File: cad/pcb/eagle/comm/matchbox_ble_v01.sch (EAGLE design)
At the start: 24 parts, among them J1 DF12-32-DS, J2 DF12-32-DS, P1 DF12-32-DP, P2 DF12-32-DP, U1 NRF8001, U5 2450BM14A0002, Y1 NX3225SA-16

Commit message: BT tweaks
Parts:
- removed TP1, TP2, TP3: TEST-POINT3X5, SparkFun-Passives:TEST-POINT3X5
- added R3, R4, R5: 0K, SparkFun-Passives:RESISTOR0805-RES
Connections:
- net N$3 renamed ANT2
- net N$6 renamed ANT1
- net ACTIVE: no longer TP1.1
- net PA9: now also R3.1
- net PB3: now also U1.SCK
- net PB4: now also U1.MISO
- net PB5: now also U1.MOSI
- net PB6: now also R4.1
- net PB7: now also R5.1
- net PC10: no longer U1.SCK
- net PC11: no longer U1.MISO
- net PC12: no longer U1.MOSI
- net RDYN: now also R3.2
- net RXD: now also R4.2; no longer TP2.1
- net TXD: now also R5.2; no longer TP3.1

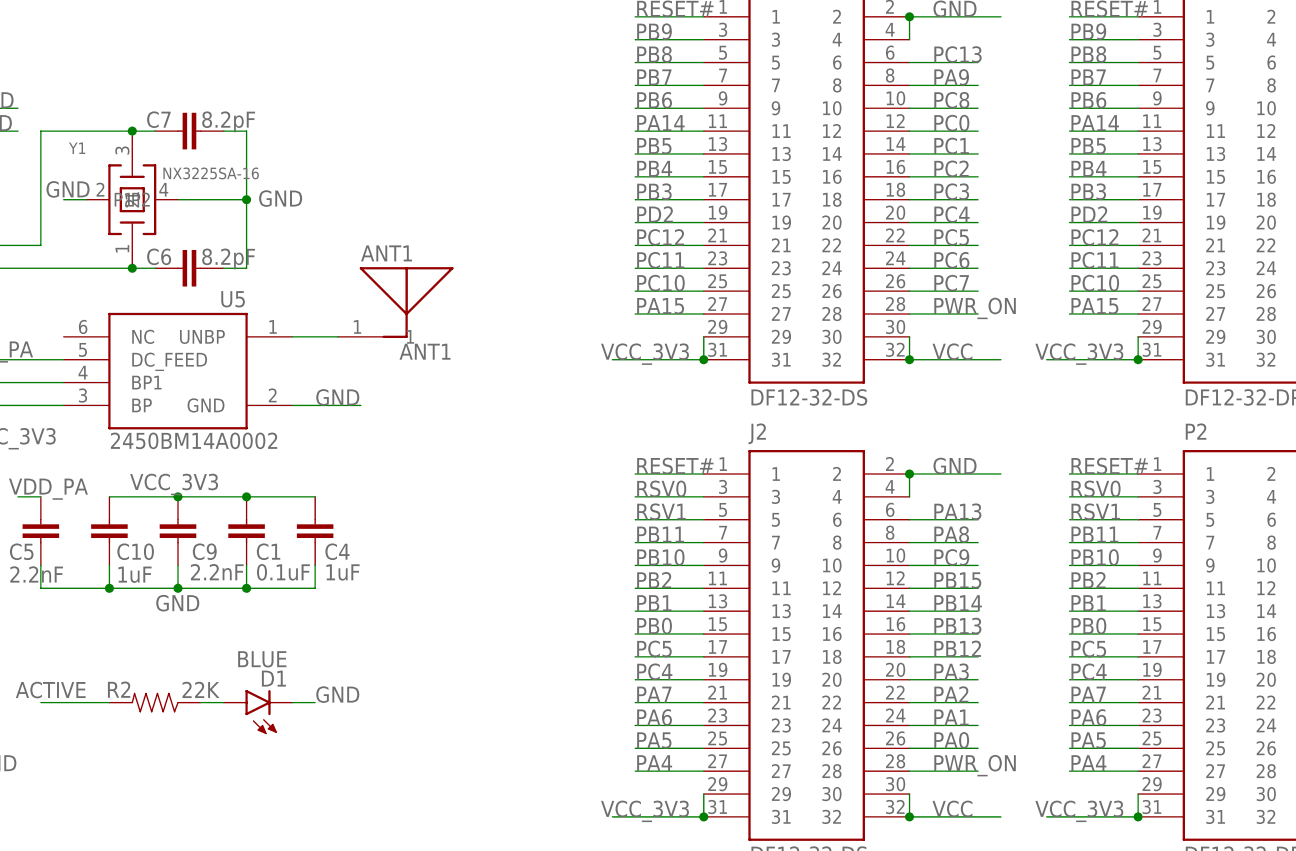
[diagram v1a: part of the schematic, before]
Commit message: Switch BLE to 40x32mm form factor
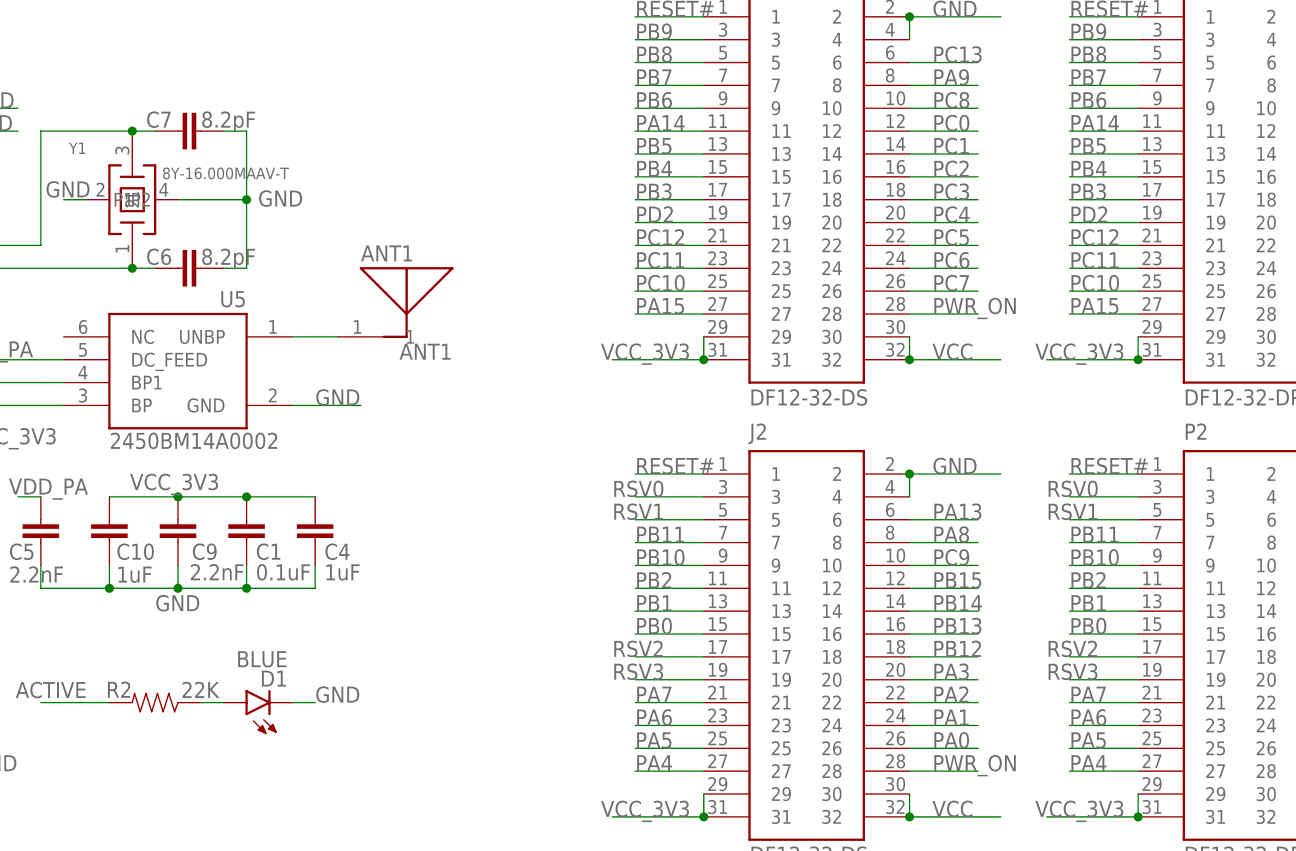
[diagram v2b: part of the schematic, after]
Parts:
- Y1: value NX3225SA-16 -> 8Y-16.000MAAV-T; device tinycircuits:AS-ITM-00228 -> micro1292:AS-ITM-00228
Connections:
- new net RSV2: J2.17, P2.17
- new net RSV3: J2.19, P2.19
- net PC4: no longer J2.19, P2.19
- net PC5: no longer J2.17, P2.17
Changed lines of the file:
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@@
 <layer number="115" name="ReferenceISLANDS" color="7" fill="1" visible="yes" active="yes"/>
 <layer number="116" name="Patch_BOT" color="7" fill="1" visible="yes" active="yes"/>
+<layer number="117" name="mPads" color="7" fill="1" visible="yes" active="yes"/>
 <layer number="118" name="Rect_Pads" color="7" fill="1" visible="yes" active="yes"/>
+<layer number="119" name="mUnrouted" color="7" fill="1" visible="yes" active="yes"/>
+<layer number="120" name="mDimension" color="7" fill="1" visible="yes" active="yes"/>
 <layer number="121" name="_tsilk" color="7" fill="1" visible="yes" active="yes"/>
 <layer number="122" name="_bsilk" color="7" fill="1" visible="yes" active="yes"/>
@@
 <layer number="128" name="_bValues" color="7" fill="1" visible="yes" active="yes"/>
 <layer number="129" name="Mask" color="7" fill="1" visible="yes" active="yes"/>
+<layer number="130" name="mbStop" color="7" fill="1" visible="yes" active="yes"/>
 <layer number="131" name="tAdjust" color="7" fill="1" visible="yes" active="yes"/>
 <layer number="132" name="bAdjust" color="7" fill="1" visible="yes" active="yes"/>
+<layer number="133" name="mtFinish" color="7" fill="1" visible="yes" active="yes"/>
+<layer number="134" name="mbFinish" color="7" fill="1" visible="yes" active="yes"/>
+<layer number="135" name="mtGlue" color="7" fill="1" visible="yes" active="yes"/>
+<layer number="136" name="mbGlue" color="7" fill="1" visible="yes" active="yes"/>
+<layer number="137" name="mtTest" color="7" fill="1" visible="yes" active="yes"/>
+<layer number="138" name="mbTest" color="7" fill="1" visible="yes" active="yes"/>
+<layer number="139" name="mtKeepout" color="7" fill="1" visible="yes" active="yes"/>
+<layer number="140" name="mbKeepout" color="7" fill="1" visible="yes" active="yes"/>
+<layer number="141" name="mtRestrict" color="7" fill="1" visible="yes" active="yes"/>
+<layer number="142" name="mbRestrict" color="7" fill="1" visible="yes" active="yes"/>
+<layer number="143" name="mvRestrict" color="7" fill="1" visible="yes" active="yes"/>
 <layer number="144" name="Drill_legend" color="7" fill="1" visible="yes" active="yes"/>
+<layer number="145" name="mHoles" color="7" fill="1" visible="yes" active="yes"/>
+<layer number="146" name="mMilling" color="7" fill="1" visible="yes" active="yes"/>
+<layer number="147" name="mMeasures" color="7" fill="1" visible="yes" active="yes"/>
+<layer number="148" name="mDocument" color="7" fill="1" visible="yes" active="yes"/>
+<layer number="149" name="mReference" color="7" fill="1" visible="yes" active="yes"/>
 <layer number="150" name="Notes" color="7" fill="1" visible="yes" active="yes"/>
 <layer number="151" name="HeatSink" color="7" fill="1" visible="yes" active="yes"/>
@@
 <layer number="154" name="FabDoc2" color="7" fill="1" visible="yes" active="yes"/>
 <layer number="155" name="FabDoc3" color="7" fill="1" visible="yes" active="yes"/>
+<layer number="191" name="mNets" color="7" fill="1" visible="yes" active="yes"/>
+<layer number="192" name="mBusses" color="7" fill="1" visible="yes" active="yes"/>
+<layer number="193" name="mPins" color="7" fill="1" visible="yes" active="yes"/>
+<layer number="194" name="mSymbols" color="7" fill="1" visible="yes" active="yes"/>
+<layer number="195" name="mNames" color="7" fill="1" visible="yes" active="yes"/>
+<layer number="196" name="mValues" color="7" fill="1" visible="yes" active="yes"/>
 <layer number="199" name="Contour" color="7" fill="1" visible="yes" active="yes"/>
 <layer number="200" name="200bmp" color="7" fill="1" visible="yes" active="yes"/>
@@
 <part name="U5" library="tinycircuits" deviceset="AS-ITM-00114" device="" value="2450BM14A0002"/>
 <part name="C5" library="SparkFun-Passives" deviceset="CAP" device="0402-CAP" value="2.2nF"/>
-<part name="Y1" library="tinycircuits" deviceset="AS-ITM-00228" device="" value="NX3225SA-16">
+<part name="Y1" library="micro1292" deviceset="AS-ITM-00228" device="" value="8Y-16.000MAAV-T">
 <attribute name="PARTNO" value="AS-ITM-00228"/>
 <attribute name="VALUE" value="8Y-16.000MAAV-T"/>
@@
 <net name="PC4" class="0">
 <segment>
-<wire x1="167.64" y1="48.26" x2="175.26" y2="48.26" width="0.1524" layer="91"/>
-<label x="167.64" y="48.26" size="1.778" layer="95"/>
-<pinref part="P2" gate="G$1" pin="19"/>
-</segment>
-<segment>
 <wire x1="198.12" y1="99.06" x2="205.74" y2="99.06" width="0.1524" layer="91"/>
 <label x="200.66" y="99.06" size="1.778" layer="95"/>
@@
 </segment>
 <segment>
-<wire x1="119.38" y1="48.26" x2="127" y2="48.26" width="0.1524" layer="91"/>
-<label x="119.38" y="48.26" size="1.778" layer="95"/>
-<pinref part="J2" gate="G$1" pin="19"/>
-</segment>
-<segment>
 <wire x1="149.86" y1="99.06" x2="157.48" y2="99.06" width="0.1524" layer="91"/>
 <label x="152.4" y="99.06" size="1.778" layer="95"/>
@@
 <net name="PC5" class="0">
 <segment>
-<wire x1="167.64" y1="50.8" x2="175.26" y2="50.8" width="0.1524" layer="91"/>
-<label x="167.64" y="50.8" size="1.778" layer="95"/>
-<pinref part="P2" gate="G$1" pin="17"/>
-</segment>
-<segment>
 <wire x1="198.12" y1="96.52" x2="205.74" y2="96.52" width="0.1524" layer="91"/>
 <label x="200.66" y="96.52" size="1.778" layer="95"/>
@@
 </segment>
 <segment>
-<wire x1="119.38" y1="50.8" x2="127" y2="50.8" width="0.1524" layer="91"/>
-<label x="119.38" y="50.8" size="1.778" layer="95"/>
-<pinref part="J2" gate="G$1" pin="17"/>
-</segment>
-<segment>
 <wire x1="149.86" y1="96.52" x2="157.48" y2="96.52" width="0.1524" layer="91"/>
 <label x="152.4" y="96.52" size="1.778" layer="95"/>
@@
 <segment>
 <wire x1="167.64" y1="68.58" x2="175.26" y2="68.58" width="0.1524" layer="91"/>
-<label x="167.64" y="68.58" size="1.778" layer="95"/>
+<label x="165.1" y="68.58" size="1.778" layer="95"/>
 <pinref part="P2" gate="G$1" pin="3"/>
 </segment>
 <segment>
 <wire x1="119.38" y1="68.58" x2="127" y2="68.58" width="0.1524" layer="91"/>
-<label x="119.38" y="68.58" size="1.778" layer="95"/>
+<label x="116.84" y="68.58" size="1.778" layer="95"/>
 <pinref part="J2" gate="G$1" pin="3"/>
 </segment>
@@
 <segment>
 <wire x1="167.64" y1="66.04" x2="175.26" y2="66.04" width="0.1524" layer="91"/>
-<label x="167.64" y="66.04" size="1.778" layer="95"/>
+<label x="165.1" y="66.04" size="1.778" layer="95"/>
 <pinref part="P2" gate="G$1" pin="5"/>
 </segment>
 <segment>
 <wire x1="119.38" y1="66.04" x2="127" y2="66.04" width="0.1524" layer="91"/>
-<label x="119.38" y="66.04" size="1.778" layer="95"/>
+<label x="116.84" y="66.04" size="1.778" layer="95"/>
 <pinref part="J2" gate="G$1" pin="5"/>
 </segment>
@@
 </segment>
 </net>
+<net name="RSV2" class="0">
+<segment>
+<wire x1="119.38" y1="50.8" x2="127" y2="50.8" width="0.1524" layer="91"/>
+<label x="116.84" y="50.8" size="1.778" layer="95"/>
+<pinref part="J2" gate="G$1" pin="17"/>
+</segment>
+<segment>
+<wire x1="167.64" y1="50.8" x2="175.26" y2="50.8" width="0.1524" layer="91"/>
+<label x="165.1" y="50.8" size="1.778" layer="95"/>
+<pinref part="P2" gate="G$1" pin="17"/>
+</segment>
+</net>
+<net name="RSV3" class="0">
+<segment>
+<wire x1="119.38" y1="48.26" x2="127" y2="48.26" width="0.1524" layer="91"/>
+<label x="116.84" y="48.26" size="1.778" layer="95"/>
+<pinref part="J2" gate="G$1" pin="19"/>
+</segment>
+<segment>
+<wire x1="167.64" y1="48.26" x2="175.26" y2="48.26" width="0.1524" layer="91"/>
+<label x="165.1" y="48.26" size="1.778" layer="95"/>
+<pinref part="P2" gate="G$1" pin="19"/>
+</segment>
+</net>

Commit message: Add VDDA supply (WIP)
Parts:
- added C8: 0.1µF, SparkFun-Capacitors:CAP0805
- added FB1: MMZ1608B121C, microbuilder:FERRITE0805
- added L4: 10µH, microbuilder:INDUCTOR_0603
- added L5: 15nH, microbuilder:INDUCTOR_0603
- added R6: 0K, SparkFun-Passives:RESISTOR0805-RES
- R2: value 22K -> 1K; device SparkFun-Passives:RESISTOR0402-RES -> SparkFun-Passives:RESISTOR0805-RES
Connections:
- new net AVDD: C8.1, FB1.P$2, L5.2, U1.AVDD, U1.AVDD1, U1.AVDD2
- new net DCC: L4.1, U1.DCC
- new net DET: R6.2, U$1.DET
- new net N$3: L4.2, L5.1
- net GND: now also C8.2
- net PB8: now also R6.1
- net VCC_3V3: now also FB1.P$1; no longer U1.AVDD, U1.AVDD1, U1.AVDD2
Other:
- moved on the sheet: D1, J1, J2, P1, P2, R2, U$1

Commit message: Final BLE board
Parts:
- removed C8: 0.1µF, SparkFun-Capacitors:CAP0805
- removed FB1: MMZ1608B121C, microbuilder:FERRITE0805
- removed L4: 10µH, microbuilder:INDUCTOR_0603
- removed L5: 15nH, microbuilder:INDUCTOR_0603
- ANT1, C2, C4, C5, C6, C7, D1, J1, J2, P1, P2, R1, R2, R3, R4, R5, R6, U$1, U1, U5, Y1: OC_NEWARK (none) -> unknown
- C1, C3: value 0.1uF -> 100nF; MF (none) -> VISHAY/SPRAGUE; MPN (none) -> 1C20Z5U104M050B; OC_NEWARK (none) -> 17F2165
- C10: value 1uF -> 100nF; MF (none) -> VISHAY/SPRAGUE; MPN (none) -> 1C20Z5U104M050B; OC_NEWARK (none) -> 17F2165
- C9: value 2.2nF -> 1nF; OC_NEWARK (none) -> unknown
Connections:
- net RDYN renamed RDY#
- removed net AVDD: C8.1, FB1.P$2, L5.2, U1.AVDD, U1.AVDD1, U1.AVDD2
- removed net DCC: L4.1, U1.DCC
- removed net N$3: L4.2, L5.1
- net GND: no longer C8.2
- net VCC_3V3: now also U1.AVDD, U1.AVDD1, U1.AVDD2; no longer FB1.P$1
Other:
- moved on the sheet: D1, R2, R3, R4, R5, R6
